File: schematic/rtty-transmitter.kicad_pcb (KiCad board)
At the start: 2 copper layers, 100 x 60 mm, 32 parts, among them J1 USB_B, J2 USBasp header, J3 Conn_Coaxial, Q1 PN2222A, U1 MCP2221AxP, U2 ATmega328P-P, U3 MCP4901, U4 MCP6022, U5 2x5 Pin Header Connector Fema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, U6 25LC1024, Y1 16 MHz, Y1 Crystal

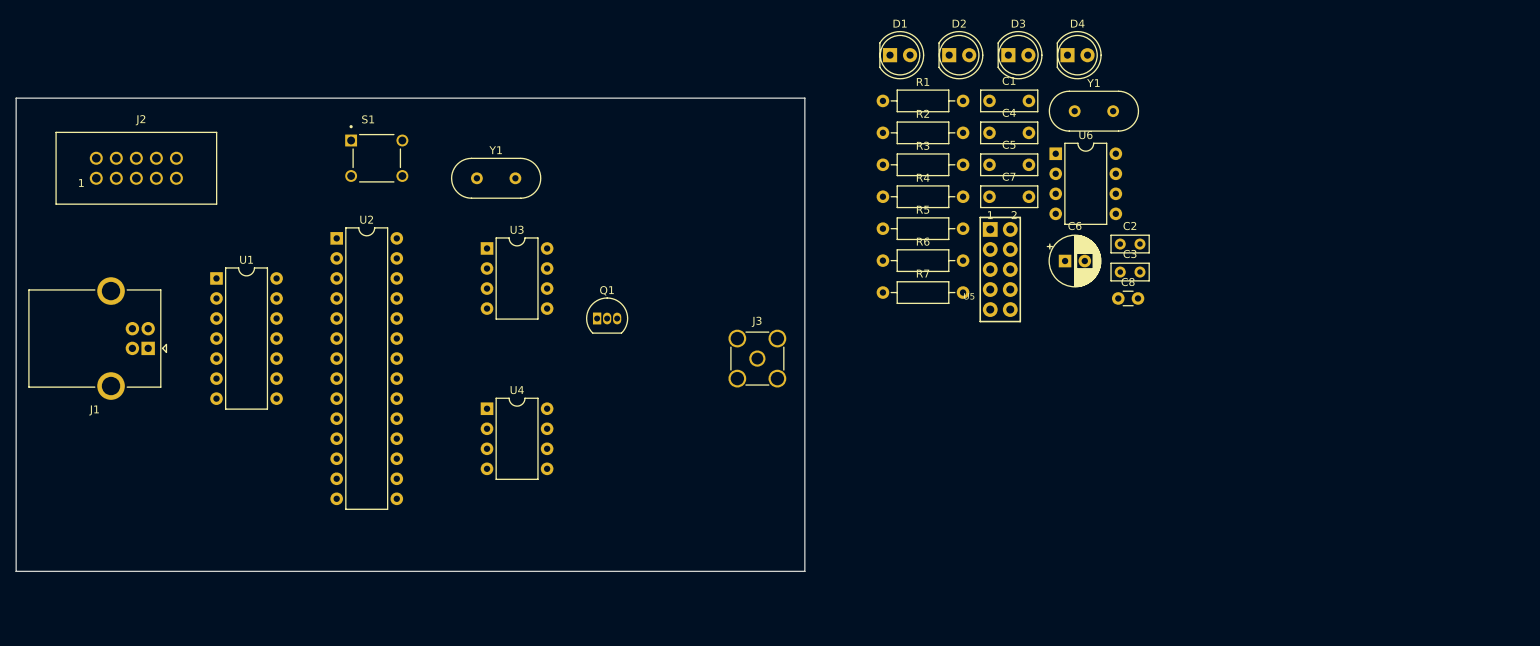
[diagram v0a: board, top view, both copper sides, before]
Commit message: Schematic: USB Type B connector symbol updated
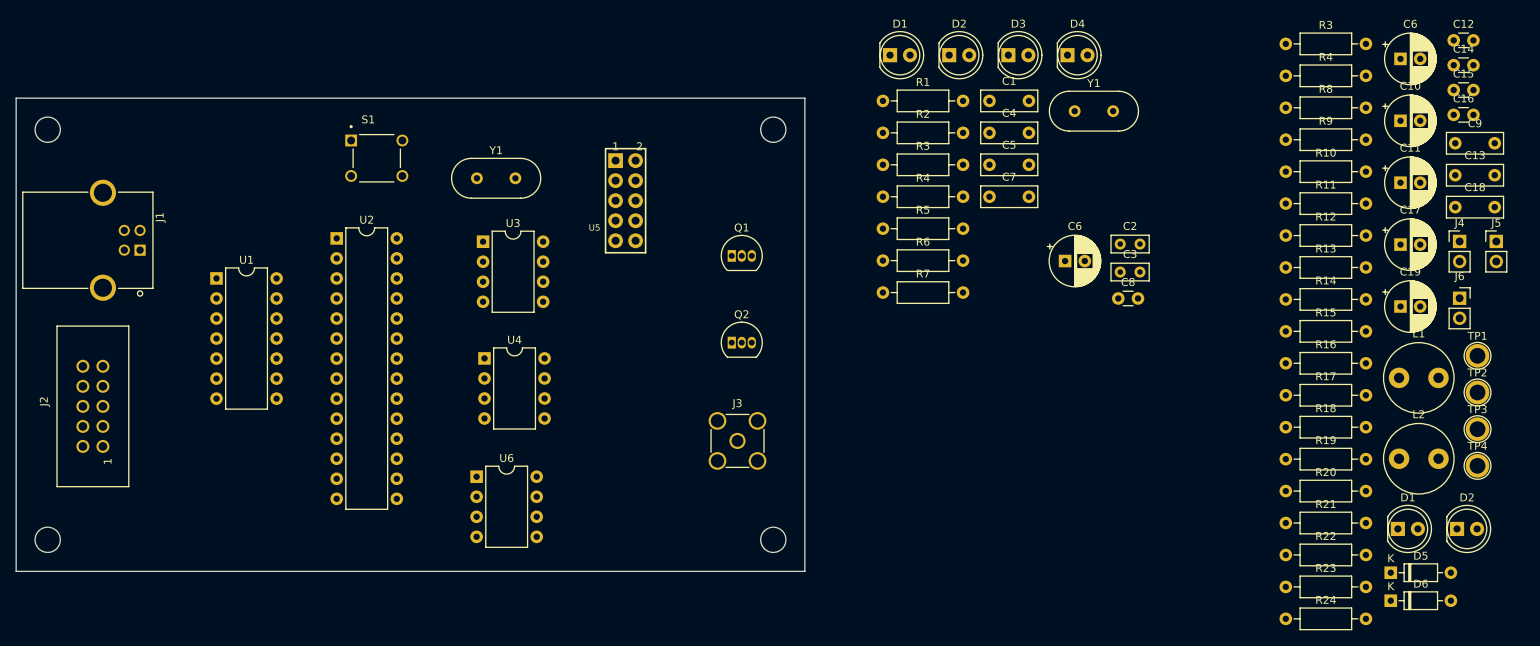
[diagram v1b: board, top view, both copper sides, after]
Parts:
- added C10: 10uF, Capacitor_THT:CP_Radial_D6.3mm_P2.50mm, F.Cu at (175.5, 2.87)
- added C11: 10uF, Capacitor_THT:CP_Radial_D6.3mm_P2.50mm, F.Cu at (175.5, 10.7)
- added C12: 100pF, Capacitor_THT:C_Disc_D3.0mm_W1.6mm_P2.50mm, F.Cu at (182.3, -7.33)
- added C13: 100nF, StockLib:C_100nF_L7.0mm_W2.5mm_P5.00mm, F.Cu at (182.5, 9.77)
- added C14: 1nF, Capacitor_THT:C_Disc_D3.0mm_W1.6mm_P2.50mm, F.Cu at (182.3, -4.18)
- added C15: 100pF, Capacitor_THT:C_Disc_D3.0mm_W1.6mm_P2.50mm, F.Cu at (182.3, -1.03)
- added C16: 100pF, Capacitor_THT:C_Disc_D3.0mm_W1.6mm_P2.50mm, F.Cu at (182.3, 2.12)
- added C17: 10uF, Capacitor_THT:CP_Radial_D6.3mm_P2.50mm, F.Cu at (175.5, 18.6)
- added C18: 100nF, StockLib:C_100nF_L7.0mm_W2.5mm_P5.00mm, F.Cu at (182.5, 13.8)
- added C19: 10uF, Capacitor_THT:CP_Radial_D6.3mm_P2.50mm, F.Cu at (175.5, 26.4)
- added C6: 10uF, Capacitor_THT:CP_Radial_D6.3mm_P2.50mm, F.Cu at (175.5, -4.98)
- added C9: 100nF, StockLib:C_100nF_L7.0mm_W2.5mm_P5.00mm, F.Cu at (182.5, 5.72)
- added D1: LED 5mm GREEN, StockLib:LED_D5.0mm_YELLOW, F.Cu at (175.2, 54.6)
- added D2: LED 5mm YELLOW, StockLib:LED_D5.0mm_YELLOW, F.Cu at (182.7, 54.6)
- added D5: 1N4148, Diode_THT:D_DO-35_SOD27_P7.62mm_Horizontal, F.Cu at (174.3, 60.2)
- added D6: 1N4148, Diode_THT:D_DO-35_SOD27_P7.62mm_Horizontal, F.Cu at (174.3, 63.7)
- added J4: Conn_01x02_Pin, Connector_PinHeader_2.54mm:PinHeader_1x02_P2.54mm_Vertical, F.Cu at (183.0, 18.2)
- added J5: Conn_01x02_Pin, Connector_PinHeader_2.54mm:PinHeader_1x02_P2.54mm_Vertical, F.Cu at (187.7, 18.2)
- added J6: Conn_01x02_Pin, Connector_PinSocket_2.54mm:PinSocket_1x02_P2.54mm_Vertical, F.Cu at (183.0, 25.4)
- added L1: 1mH, Inductor_THT:L_Radial_D8.7mm_P5.00mm_Fastron_07HCP, F.Cu at (175.3, 35.5)
- added L2: 330uH, Inductor_THT:L_Radial_D8.7mm_P5.00mm_Fastron_07HCP, F.Cu at (175.3, 45.7)
- added MH1: MountingHole_3.2mm_M3_DIN965, MountingHole:MountingHole_3.2mm_M3_DIN965, F.Cu at (4.00, 4.00)
- added MH2: MountingHole_3.2mm_M3_DIN965, MountingHole:MountingHole_3.2mm_M3_DIN965, F.Cu at (96.0, 4.00)
- added MH3: MountingHole_3.2mm_M3_DIN965, MountingHole:MountingHole_3.2mm_M3_DIN965, F.Cu at (4.00, 56.0)
- added MH4: MountingHole_3.2mm_M3_DIN965, MountingHole:MountingHole_3.2mm_M3_DIN965, F.Cu at (96.0, 56.0)
- added Q2: PN2222A, Package_TO_SOT_THT:TO-92_Inline, F.Cu at (90.7, 31.0)
- added R10: 220R, StockLib:R_10k_Axial_DIN0207, F.Cu at (161.0, 9.32)
- added R11: 100R, StockLib:R_10k_Axial_DIN0207, F.Cu at (161.0, 13.4)
- added R12: 22k, StockLib:R_10k_Axial_DIN0207, F.Cu at (161.0, 17.4)
- added R13: 10k, StockLib:R_10k_Axial_DIN0207, F.Cu at (161.0, 21.5)
- added R14: 1.5k, StockLib:R_10k_Axial_DIN0207, F.Cu at (161.0, 25.5)
- added R15: 1.5k, StockLib:R_10k_Axial_DIN0207, F.Cu at (161.0, 29.6)
- added R16: 4.7k, StockLib:R_10k_Axial_DIN0207, F.Cu at (161.0, 33.6)
- added R17: 15k, StockLib:R_10k_Axial_DIN0207, F.Cu at (161.0, 37.7)
- added R18: 10k, StockLib:R_10k_Axial_DIN0207, F.Cu at (161.0, 41.7)
- added R19: 10k, StockLib:R_10k_Axial_DIN0207, F.Cu at (161.0, 45.8)
- added R20: 10k, StockLib:R_10k_Axial_DIN0207, F.Cu at (161.0, 49.8)
- added R21: 10k, StockLib:R_10k_Axial_DIN0207, F.Cu at (161.0, 53.9)
- added R22: 10k, StockLib:R_10k_Axial_DIN0207, F.Cu at (161.0, 57.9)
- added R23: 10k, StockLib:R_10k_Axial_DIN0207, F.Cu at (161.0, 62.0)
- added R24: 2.2k, StockLib:R_10k_Axial_DIN0207, F.Cu at (161.0, 66.0)
- added R3: 470R, StockLib:R_470_Axial_DIN0207, F.Cu at (161.0, -6.88)
- added R4: 470R, StockLib:R_470_Axial_DIN0207, F.Cu at (161.0, -2.83)
- added R8: 10k, StockLib:R_10k_Axial_DIN0207, F.Cu at (161.0, 1.22)
- added R9: 470R, StockLib:R_10k_Axial_DIN0207, F.Cu at (161.0, 5.27)
- added TP1: TestPoint, TestPoint:TestPoint_Plated_Hole_D2.0mm, F.Cu at (185.3, 32.7)
- added TP2: TestPoint, TestPoint:TestPoint_Plated_Hole_D2.0mm, F.Cu at (185.3, 37.3)
- added TP3: TestPoint, TestPoint:TestPoint_Plated_Hole_D2.0mm, F.Cu at (185.3, 42.0)
- added TP4: TestPoint, TestPoint:TestPoint_Plated_Hole_D2.0mm, F.Cu at (185.3, 46.6)
- D4: footprint StockLib:LED_D5.0mm_WHITE -> StockLib:LED_D5.0mm_YELLOW
- J1: value USB_B -> USB Type B Connector; footprint Connector_USB:USB_B_OST_USB-B1HSxx_Horizontal -> StockLib:USB Type B Connector
- moved U6 84.1 mm to (58.4, 48.0)
- moved U5 48.3 mm to (77.3, 13.0)
- moved J2 30.7 mm to (9.73, 39.1), turned to 90 degrees
- moved Q1 18.8 mm to (90.7, 20.0)
- moved J1 12.5 mm to (15.7, 19.3), turned to -90 degrees
- moved J3 10.7 mm to (91.5, 43.5)
- moved U4 6.39 mm to (59.4, 33.0)
- moved U3 0.99 mm to (59.2, 18.2)
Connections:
- net AUDIO SIGNAL renamed Net-(C10-Pad1)
- C4 pad 1: GND -> +5V
- C4 pad 2: +5V -> GND
- J3 pad 1: unconnected-(J3-In-Pad1) -> Net-(J3-In)
- J3 pad 2: unconnected-(J3-Ext-Pad2) -> GND
- Q1 pad 1: unconnected-(Q1-E-Pad1) -> Net-(Q1-E)
- Q1 pad 2: unconnected-(Q1-B-Pad2) -> Net-(Q1-B)
- Q1 pad 3: unconnected-(Q1-C-Pad3) -> Net-(Q1-C)
- R7 pad 1: Net-(U2-PC5) -> Net-(U2-PD7)
- U1 pad 5: Net-(U1-URx) -> Net-(J5-Pin_2)
- U1 pad 6: Net-(U1-UTx) -> Net-(J4-Pin_1)
- U2 pad 11: unconnected-(U2-PD5-Pad11) -> Net-(U2-PD5)
- U2 pad 12: unconnected-(U2-PD6-Pad12) -> Net-(U2-PD6)
- U2 pad 13: unconnected-(U2-PD7-Pad13) -> Net-(U2-PD7)
- U2 pad 2: Net-(U1-UTx) -> Net-(J4-Pin_2)
- U2 pad 24: Net-(U2-PC1) -> unconnected-(U2-PC1-Pad24)
- U2 pad 25: Net-(U2-PC2) -> unconnected-(U2-PC2-Pad25)
- U2 pad 3: Net-(U1-URx) -> Net-(J5-Pin_1)
- U2 pad 4: unconnected-(U2-PD2-Pad4) -> Net-(U2-PD2)
- U2 pad 5: unconnected-(U2-PD3-Pad5) -> Net-(U2-PD3)
- U2 pad 6: unconnected-(U2-PD4-Pad6) -> Net-(U2-PD4)
- U4 pad 1: unconnected-(U4-Pad1) -> CARRIER WAVE
- U4 pad 2: unconnected-(U4A---Pad2) -> Net-(D5-K)
- U4 pad 3: unconnected-(U4A-+-Pad3) -> Net-(U4A-+)
- U4 pad 4: unconnected-(U4C-V--Pad4) -> GND
- U4 pad 5: unconnected-(U4B-+-Pad5) -> Net-(U4B-+)
- U4 pad 6: unconnected-(U4B---Pad6) -> Net-(U4B--)
- U4 pad 7: unconnected-(U4-Pad7) -> BUFFERED AUDIO
- U4 pad 8: unconnected-(U4C-V+-Pad8) -> +5V
- U5 pad 1: Net-(U2-PC0) -> Net-(U2-PD2)
- U5 pad 3: Net-(U2-PC1) -> Net-(U2-PD3)
- U5 pad 5: Net-(U2-PC2) -> Net-(U2-PD4)
- U5 pad 7: Net-(U2-PC3) -> Net-(U2-PD5)
- U5 pad 9: Net-(U2-PC4) -> Net-(U2-PD6)
- U6 pad 1: unconnected-(U6-~{CS}-Pad1) -> Net-(U2-PC0)
- U6 pad 2: unconnected-(U6-MISO-Pad2) -> Net-(U2-PC5)
- U6 pad 5: unconnected-(U6-MOSI-Pad5) -> Net-(U2-PC3)
- U6 pad 6: unconnected-(U6-SCK-Pad6) -> Net-(U2-PC4)
- U6 pad 7: GND -> +5V

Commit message: PCB: Components updated
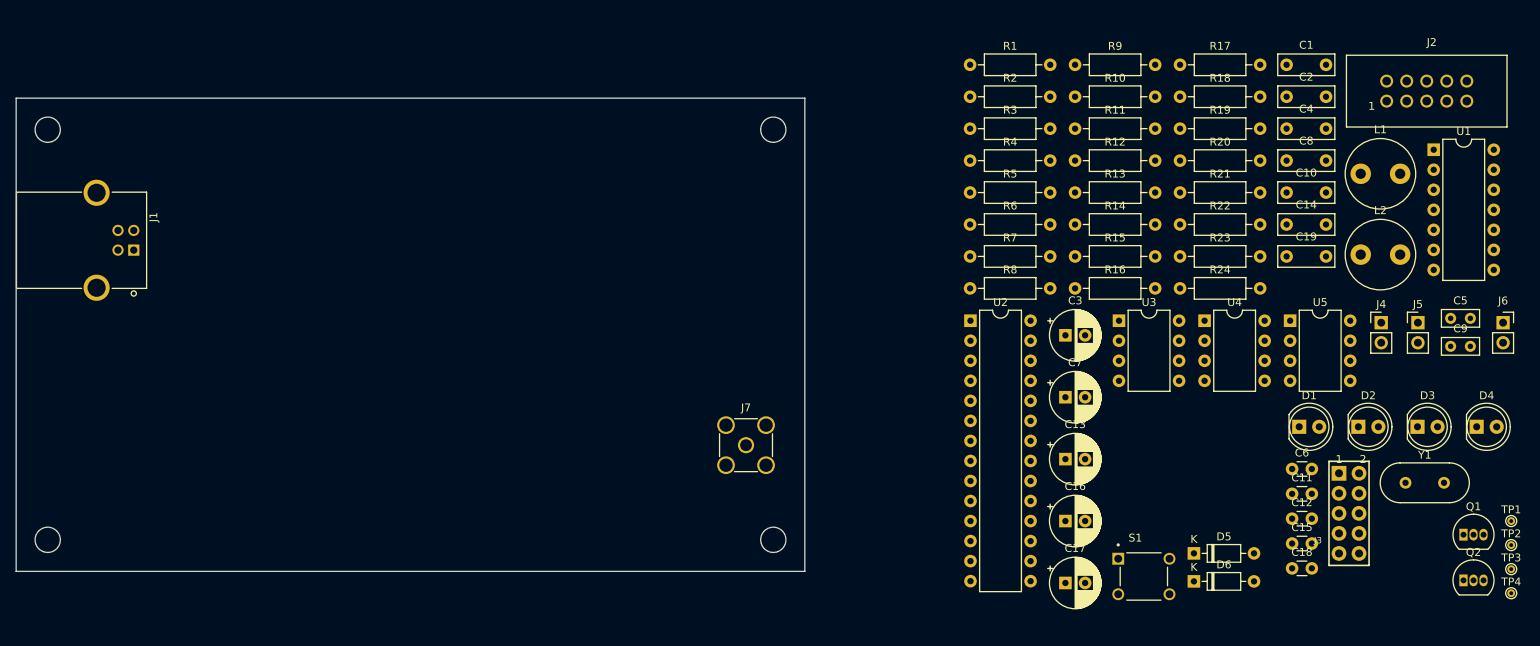
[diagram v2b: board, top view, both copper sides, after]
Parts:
- removed the C6 at (175.5, -4.98)
- removed the C6 at (133.0, 20.6)
- removed the D1 at (110.8, -5.45)
- removed the D1 at (175.2, 54.6)
- removed the D2 at (118.3, -5.45)
- removed the D2 at (182.7, 54.6)
- removed the R3 at (161.0, -6.88)
- removed the R3 at (109.9, 8.45)
- removed the R4 at (161.0, -2.83)
- removed the R4 at (109.9, 12.5)
- removed U6: 25LC1024, Package_DIP:DIP-8_W7.62mm
- removed the Y1 at (58.4, 10.2)
- removed the Y1 at (134.2, 1.65)
- added C6: 100pF, Capacitor_THT:C_Disc_D3.0mm_W1.6mm_P2.50mm, F.Cu at (161.8, 47.0)
- added D1: LED 5mm YELLOW, StockLib:LED_D5.0mm_YELLOW, F.Cu at (162.7, 41.7)
- added D2: LED 5mm GREEN, StockLib:LED_D5.0mm_YELLOW, F.Cu at (170.2, 41.7)
- added J7: Conn_Coaxial, Connector_Coaxial:SMA_Amphenol_901-144_Vertical, F.Cu at (92.5, 44.0)
- added R3: 470R, StockLib:R_470_Axial_DIN0207, F.Cu at (121.0, 3.87)
- added R4: 470R, StockLib:R_470_Axial_DIN0207, F.Cu at (121.0, 7.92)
- added Y1: 16 MHz, Crystal:Crystal_HC49-U_Vertical, F.Cu at (176.2, 48.8)
- C1: value 470nF -> 100nF
- C10, C19: value 10uF -> 100nF; footprint Capacitor_THT:CP_Radial_D6.3mm_P2.50mm -> StockLib:C_100nF_L7.0mm_W2.5mm_P5.00mm
- C11: value 10uF -> 10nF; footprint Capacitor_THT:CP_Radial_D6.3mm_P2.50mm -> Capacitor_THT:C_Disc_D3.0mm_W1.6mm_P2.50mm
- C12: value 100pF -> 1nF
- C13, C7: value 100nF -> 10uF; footprint StockLib:C_100nF_L7.0mm_W2.5mm_P5.00mm -> Capacitor_THT:CP_Radial_D6.3mm_P2.50mm
- C14: value 1nF -> 100nF; footprint Capacitor_THT:C_Disc_D3.0mm_W1.6mm_P2.50mm -> StockLib:C_100nF_L7.0mm_W2.5mm_P5.00mm
- C16: value 100pF -> 10uF; footprint Capacitor_THT:C_Disc_D3.0mm_W1.6mm_P2.50mm -> Capacitor_THT:CP_Radial_D6.3mm_P2.50mm
- C18: value 100nF -> 100pF; footprint StockLib:C_100nF_L7.0mm_W2.5mm_P5.00mm -> Capacitor_THT:C_Disc_D3.0mm_W1.6mm_P2.50mm
- C2: value 22pF -> 470nF; footprint Capacitor_THT:C_Rect_L4.6mm_W2.0mm_P2.50mm_MKS02_FKP02 -> StockLib:C_100nF_L7.0mm_W2.5mm_P5.00mm
- C3: value 22pF -> 10uF; footprint Capacitor_THT:C_Rect_L4.6mm_W2.0mm_P2.50mm_MKS02_FKP02 -> Capacitor_THT:CP_Radial_D6.3mm_P2.50mm
- C5, C9: value 100nF -> 22pF; footprint StockLib:C_100nF_L7.0mm_W2.5mm_P5.00mm -> Capacitor_THT:C_Rect_L4.6mm_W2.0mm_P2.50mm_MKS02_FKP02
- C8: value 10nF -> 100nF; footprint Capacitor_THT:C_Disc_D3.0mm_W1.6mm_P2.50mm -> StockLib:C_100nF_L7.0mm_W2.5mm_P5.00mm
- J3: value Conn_Coaxial -> 2x5 Pin Header Connector Female; footprint Connector_Coaxial:SMA_Amphenol_901-144_Vertical -> StockLib:2x5 Pin Header Connector Female
- R12: value 22k -> 1k; footprint StockLib:R_10k_Axial_DIN0207 -> StockLib:R_1k_Axial_DIN0207
- R15: value 1.5k -> 10k
- R16: value 4.7k -> 10k
- R17: value 15k -> 2.2k
- R19: value 10k -> 4.7k
- R22: value 10k -> 15k
- R23: value 10k -> 1.5k
- R24: value 2.2k -> 10k
- R6: value 1k -> 470R; footprint StockLib:R_1k_Axial_DIN0207 -> StockLib:R_470_Axial_DIN0207
- R7: value 470R -> 22k; footprint StockLib:R_470_Axial_DIN0207 -> StockLib:R_10k_Axial_DIN0207
- TP1: value TestPoint -> Virtual Ground; footprint TestPoint:TestPoint_Plated_Hole_D2.0mm -> TestPoint:TestPoint_THTPad_D1.0mm_Drill0.5mm
- TP2: value TestPoint -> GND; footprint TestPoint:TestPoint_Plated_Hole_D2.0mm -> TestPoint:TestPoint_THTPad_D1.0mm_Drill0.5mm
- TP3: value TestPoint -> Carrier Wave; footprint TestPoint:TestPoint_Plated_Hole_D2.0mm -> TestPoint:TestPoint_THTPad_D1.0mm_Drill0.5mm
- TP4: value TestPoint -> Buffered Audio; footprint TestPoint:TestPoint_Plated_Hole_D2.0mm -> TestPoint:TestPoint_THTPad_D1.0mm_Drill0.5mm
- U4: value MCP6022 -> 25LC1024
- U5: value 2x5 Pin Header Connector Female -> MCP6022; footprint StockLib:2x5 Pin Header Connector Female -> Package_DIP:DIP-8_W7.62mm
- moved J2 173.8 mm to (178.8, -0.89), turned to 0 degrees
- moved U1 155.2 mm to (179.7, 6.54)
- moved S1 110.8 mm to (143.0, 60.6)
- moved Q1 99.3 mm to (183.5, 55.4)
- moved Q2 97.6 mm to (183.5, 61.1)
- moved U4 91.4 mm to (150.7, 28.2)
- moved U5 85.6 mm to (161.5, 28.2)
- moved U3 81.3 mm to (139.8, 28.2)
- moved U2 81.0 mm to (121.0, 28.2)
- moved J3 78.1 mm to (169.0, 52.6)
- moved C16 71.2 mm to (133.0, 53.6)
- moved D3 70.1 mm to (177.7, 41.7)
- moved D4 70.1 mm to (185.2, 41.7)
- moved C12 64.0 mm to (161.8, 53.3)
- moved C5 61.6 mm to (181.9, 27.9)
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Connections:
- C1 pad 1: Net-(U1-VUSB) -> GND
- C1 pad 2: GND -> +5V
- C10 pad 1: Net-(C10-Pad1) -> Net-(Q1-C)
- C10 pad 2: AUDIO SIGNAL -> Net-(C10-Pad2)
- C11 pad 1: BUFFERED AUDIO -> GND
- C11 pad 2: Net-(Q2-B) -> Net-(C11-Pad2)
- C12 pad 1: Net-(Q1-B) -> Net-(C10-Pad2)
- C12 pad 2: CARRIER WAVE -> GND
- C13 pad 1: Net-(Q1-C) -> Net-(C11-Pad2)
- C13 pad 2: Net-(C13-Pad2) -> AUDIO SIGNAL
- C14 pad 1: Net-(C13-Pad2) -> +5V
- C15 pad 1: Net-(U4A-+) -> Net-(U5A-+)
- C16 pad 2: Net-(U4A-+) -> AUDIO SIGNAL
- C18 pad 1: +5V -> Net-(C18-Pad1)
- C18 pad 2: GND -> Net-(U5A-+)
- C19 pad 1: Net-(C19-Pad1) -> +5V
- C19 pad 2: AUDIO SIGNAL -> GND
- C2 pad 1: Net-(U2-XTAL1/PB6) -> Net-(U1-VUSB)
- C3 pad 1: Net-(U2-XTAL2/PB7) -> +5V
- C5 pad 1: GND -> Net-(U2-XTAL1/PB6)
- C5 pad 2: +5V -> GND
- C7 pad 1: GND -> BUFFERED AUDIO
- C7 pad 2: +5V -> Net-(Q2-B)
- C8 pad 2: Net-(C10-Pad1) -> +5V
- C9 pad 1: +5V -> Net-(U2-XTAL2/PB7)
- J3 pad 1: Net-(J3-In) -> Net-(U2-PD2)
- L2 pad 1: Net-(C13-Pad2) -> Net-(C10-Pad2)
- L2 pad 2: Net-(J3-In) -> Net-(J7-In)
- R12 pad 1: Net-(Q1-B) -> Net-(U3-Vout)
- R12 pad 2: +5V -> Net-(C11-Pad2)
- R13 pad 2: Net-(Q1-B) -> AUDIO SIGNAL
- R14 pad 1: Net-(U4A-+) -> Net-(U5A-+)
- R15 pad 1: Net-(C16-Pad1) -> VIRTUAL GROUND
- R15 pad 2: CARRIER WAVE -> +5V
- R16 pad 1: Net-(D5-K) -> GND
- R17 pad 1: Net-(D5-K) -> VIRTUAL GROUND
- R17 pad 2: CARRIER WAVE -> Net-(U5B-+)
- R18 pad 1: VIRTUAL GROUND -> Net-(U5B--)
- R18 pad 2: +5V -> VIRTUAL GROUND
- R19 pad 1: GND -> Net-(D5-K)
- R20 pad 1: CARRIER WAVE -> Net-(U5B-+)
- R20 pad 2: Net-(D5-A) -> Net-(C16-Pad1)
- R21 pad 1: Net-(U4B-+) -> BUFFERED AUDIO
- R21 pad 2: Net-(C19-Pad1) -> Net-(U5B--)
- R22 pad 1: Net-(U4B--) -> Net-(D5-K)
- R22 pad 2: VIRTUAL GROUND -> CARRIER WAVE
- R23 pad 1: BUFFERED AUDIO -> Net-(C18-Pad1)
- R23 pad 2: Net-(U4B--) -> CARRIER WAVE
- R24 pad 1: VIRTUAL GROUND -> CARRIER WAVE
- R24 pad 2: Net-(U4B-+) -> Net-(D5-A)
- R6 pad 1: Net-(U3-Vout) -> Net-(U2-PD7)
- R6 pad 2: Net-(C10-Pad1) -> Net-(D4-A)
- R7 pad 1: Net-(U2-PD7) -> Net-(Q1-B)
- R7 pad 2: Net-(D4-A) -> +5V
- R8 pad 2: AUDIO SIGNAL -> Net-(Q1-B)
- TP1 pad 1: CARRIER WAVE -> VIRTUAL GROUND
- TP2 pad 1: BUFFERED AUDIO -> GND
- TP3 pad 1: VIRTUAL GROUND -> CARRIER WAVE
- TP4 pad 1: GND -> BUFFERED AUDIO
- U4 pad 1: CARRIER WAVE -> Net-(U2-PC0)
- U4 pad 2: Net-(D5-K) -> Net-(U2-PC5)
- U4 pad 3: Net-(U4A-+) -> +5V
- U4 pad 5: Net-(U4B-+) -> Net-(U2-PC3)
- U4 pad 6: Net-(U4B--) -> Net-(U2-PC4)
- U4 pad 7: BUFFERED AUDIO -> +5V
- U5 pad 1: Net-(U2-PD2) -> CARRIER WAVE
- U5 pad 2: GND -> Net-(D5-K)
- U5 pad 3: Net-(U2-PD3) -> Net-(U5A-+)
- U5 pad 5: Net-(U2-PD4) -> Net-(U5B-+)
- U5 pad 6: GND -> Net-(U5B--)
- U5 pad 7: Net-(U2-PD5) -> BUFFERED AUDIO
- U5 pad 8: GND -> +5V

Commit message: PCB: SMA connector updated
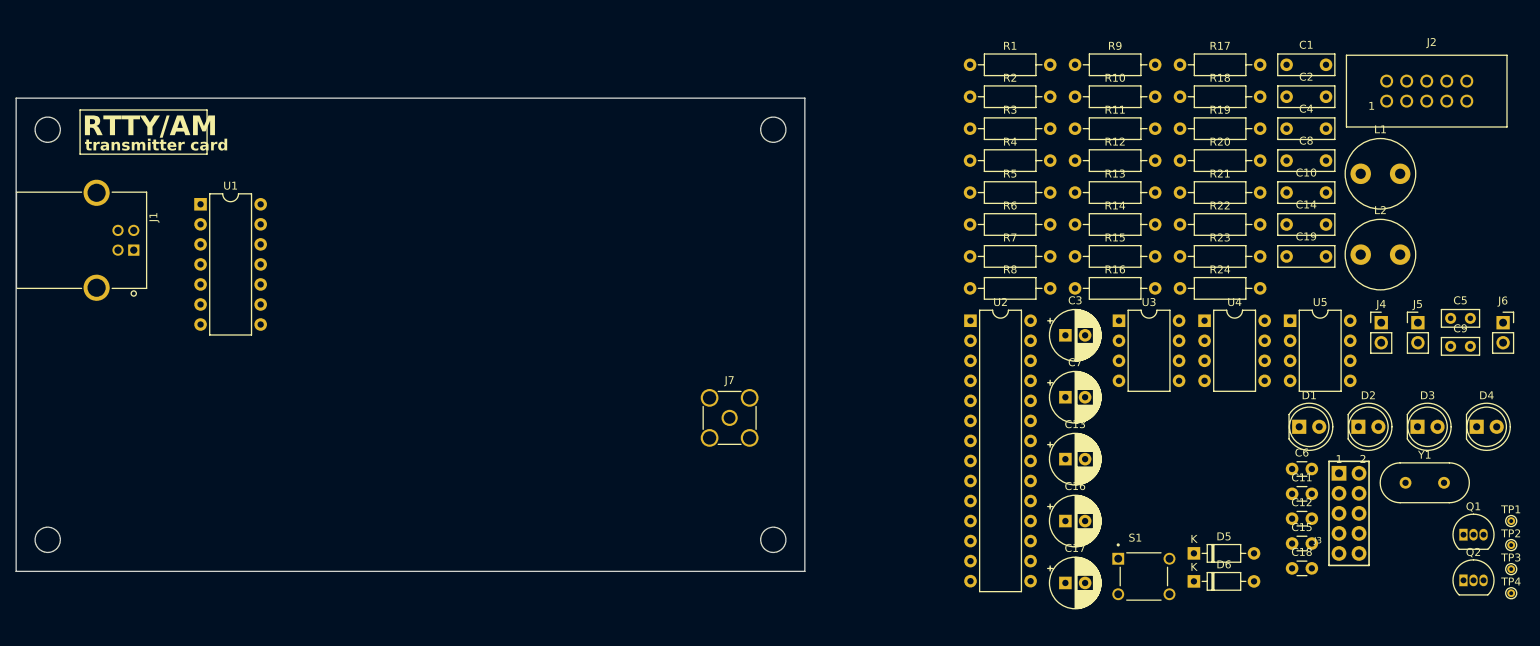
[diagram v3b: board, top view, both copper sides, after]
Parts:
- J7: value Conn_Coaxial -> SMA Vertical Female; footprint Connector_Coaxial:SMA_Amphenol_901-144_Vertical -> StockLib:SMA Vertical Female
- moved U1 156.5 mm to (23.4, 13.5)
- moved J7 4.04 mm to (90.5, 40.5)
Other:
- board text added: "RTTY/AM"
- board text added: "transmitter card"

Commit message: PCB: PCB layout updated
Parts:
- moved C1 161.9 mm to (2.79, 29.7)
- moved J5 157.3 mm to (21.6, 47.2), turned to -90 degrees
- moved J4 154.9 mm to (19.1, 44.7), turned to 90 degrees
- moved D3 154.0 mm to (27.9, 5.59)
- moved C2 152.8 mm to (11.2, 29.7)
- moved D1 150.9 mm to (12.4, 55.9)
- moved D2 150.4 mm to (20.5, 55.9)
- moved C5 149.9 mm to (32.0, 30.7)
- moved C9 143.0 mm to (38.9, 30.7)
- moved Y1 142.4 mm to (34.4, 35.3)
- moved S1 137.6 mm to (6.04, 47.0)
- moved J3 135.0 mm to (34.0, 54.6), turned to -90 degrees
- moved J2 128.2 mm to (50.9, 6.86)
- moved C4 127.5 mm to (34.3, 18.0)
- moved D4 126.5 mm to (59.4, 55.9), turned to 180 degrees
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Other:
- board size 100 x 60 mm -> 120 x 60 mm
- board text added: "(GPIO5)"
- board text added: "2026 B. MARKUS"
- board text added: "25LC1024"
- board text added: "5V"
- board text added: "ANTENNA OUT"
- board text added: "ATMEGA328P"
- board text added: "AUDIO SIGNAL"
- board text added: "BUFFERED AUDIO"
- board text added: "CARRIER WAVE"
- board text added: "GND"
- board text added: "GPIO PINS"
- board text added: "GPIO0"
- board text added: "GPIO1"
- board text added: "GPIO2"
- board text added: "GPIO3"
- board text added: "GPIO4"
- board text added: "MCP2221A"
- board text added: "MCP4901"
- board text added: "MCP6022"
- board text added: "MCP_RX"
- board text added: "MCP_TX"
- board text added: "MISO"
- board text added: "MOSI"
- board text added: "NC"
- board text added: "OUT"
- board text added: "POWER"
- board text added: "RESET"
- board text added: "RTTY/AM TRANSMITTER CARD V1.0"
- board text added: "RX"
- board text added: "SCK"
- board text added: "STATUS"
- board text added: "TX"
- board text added: "UART_RX"
- board text added: "UART_TX"
- board text added: "USBasp"
- board text added: "VIRTUAL GROUND"
